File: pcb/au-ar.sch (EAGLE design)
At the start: 44 parts, among them U1 TPD12S520DBTR, U2 TPD12S521DBTR

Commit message: rearranged hdmi ports. removed end mounting holes to make room for dual ports on the end. added footprint for spi flash and added to schematic.
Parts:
- added R5: 47k, rcl:R-US_R0603
- added U$1: W25Q80DVSNIG, TDP12S521:W25Q80DVSNIG
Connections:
- net N$11 renamed SCL1_FPGA
- net N$12 renamed SDA1_FPGA
- net N$15 renamed HP1_FPGA
- removed net N$16: U2.5V_SUPPLY
- removed net N$17: U2.LV_SUPPLY
- removed net N$2: B1C.1
- removed net N$40: U1.5V_SUPPLY
- removed net N$41: U1.LV_SUPPLY
- removed net N$42: U1.CE_REMOTE_IN, U1.GND_2, U1.TMDS_GND_2, U1.TMDS_GND_3, U1.TMDS_GND_4, U1.TMDS_GND_5
- removed net N$43: U1.ESD_BYP, U1.GND, U1.TMDS_GND, U1.TMDS_GND_6, U1.TMDS_GND_7, U1.TMDS_GND_8
- removed net PIN: B1A.1
- new net 5V: B1A.1, B1A.50, B1B.1, B1B.50, B1C.1, B1C.50, B1D.1, B1D.50, U1.5V_SUPPLY, U2.5V_SUPPLY
- new net HP2_FPGA: U1.HOTPLUG_DET_IN
- new net SCL2_FPGA: U1.DDC_CLK_IN
- new net SDA2_FPGA: U1.DDC_DAT_IN
- new net SPI_CLK: U$1.CLK
- new net SPI_DI: U$1.DI
- new net SPI_DO: U$1.DO
- net 3V3: now also B1A.13, B1A.19, B1A.25, B1A.26, B1A.32, B1A.38, B1A.44, B1A.7, B1B.13, B1B.19, B1B.25, B1B.26, B1B.32, B1B.38, B1B.44, B1B.7, B1C.13, B1C.19, B1C.25, B1C.26, B1C.32, B1C.38, B1C.44, B1C.7, B1D.13, B1D.19, B1D.25, B1D.26, B1D.32, B1D.38, B1D.44, B1D.7, R5.2, U$1.HOLD, U$1.VCC, U$1.WP, U1.LV_SUPPLY, U2.LV_SUPPLY
- net CLK1_N: now also B1B.34
- net CLK1_P: now also B1B.33
- net CLK2_N: now also B1B.40
- net CLK2_P: now also B1B.39
- net D01_N: now also B1B.17
- net D01_P: now also B1B.18
- net D02_N: now also B1B.11
- net D02_P: now also B1B.12
- net D11_N: now also B1B.31
- net D11_P: now also B1B.30
- net D12_N: now also B1B.37
- net D12_P: now also B1B.36
- net D21_N: now also B1B.20
- net D21_P: now also B1B.21
- net D22_N: now also B1B.14
- net D22_P: now also B1B.15
- net GND: now also B1A.10, B1A.16, B1A.22, B1A.29, B1A.35, B1A.4, B1A.41, B1A.47, B1B.10, B1B.16, B1B.22, B1B.29, B1B.35, B1B.4, B1B.41, B1B.47, B1C.10, B1C.16, B1C.22, B1C.29, B1C.35, B1C.4, B1C.41, B1C.47, B1D.10, B1D.16, B1D.22, B1D.29, B1D.35, B1D.4, B1D.41, B1D.47, U$1.GND, U1.CE_REMOTE_IN, U1.ESD_BYP, U1.GND, U1.GND_2, U1.TMDS_GND, U1.TMDS_GND_2, U1.TMDS_GND_3, U1.TMDS_GND_4, U1.TMDS_GND_5, U1.TMDS_GND_6, U1.TMDS_GND_7, U1.TMDS_GND_8
- net LINE_1_1: now also B1A.24
- net LINE_1_2: now also B1A.21
- net LINE_1_3: now also B1A.18
- net LINE_1_4: now also B1A.15
- net LINE_2_1: now also B1A.12
- net LINE_2_2: now also B1A.9
- net LINE_2_3: now also B1A.6
- net LINE_2_4: now also B1A.3
- net N$1: now also R5.1, U$1.CS; no longer B1B.1

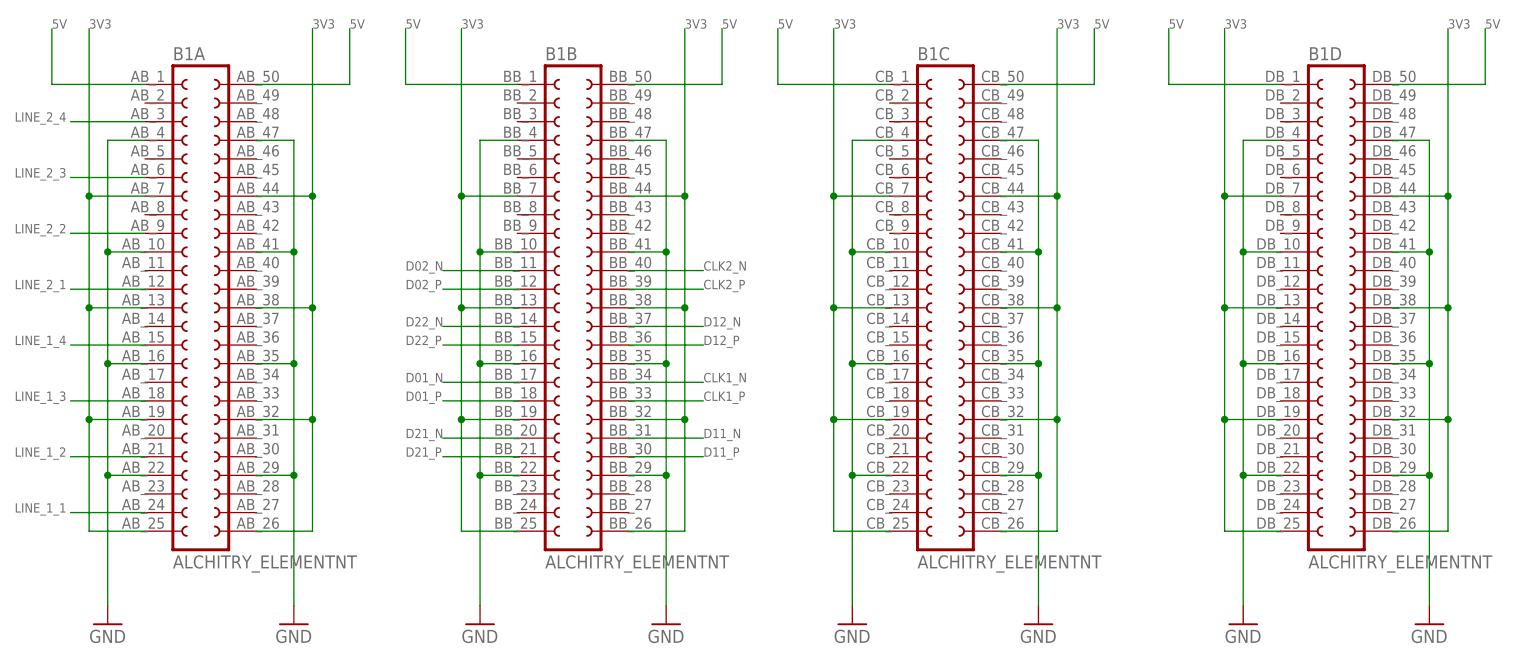
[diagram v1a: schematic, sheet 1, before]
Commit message: added remaining connections in schematic for spi flash and hdmi ddc bus
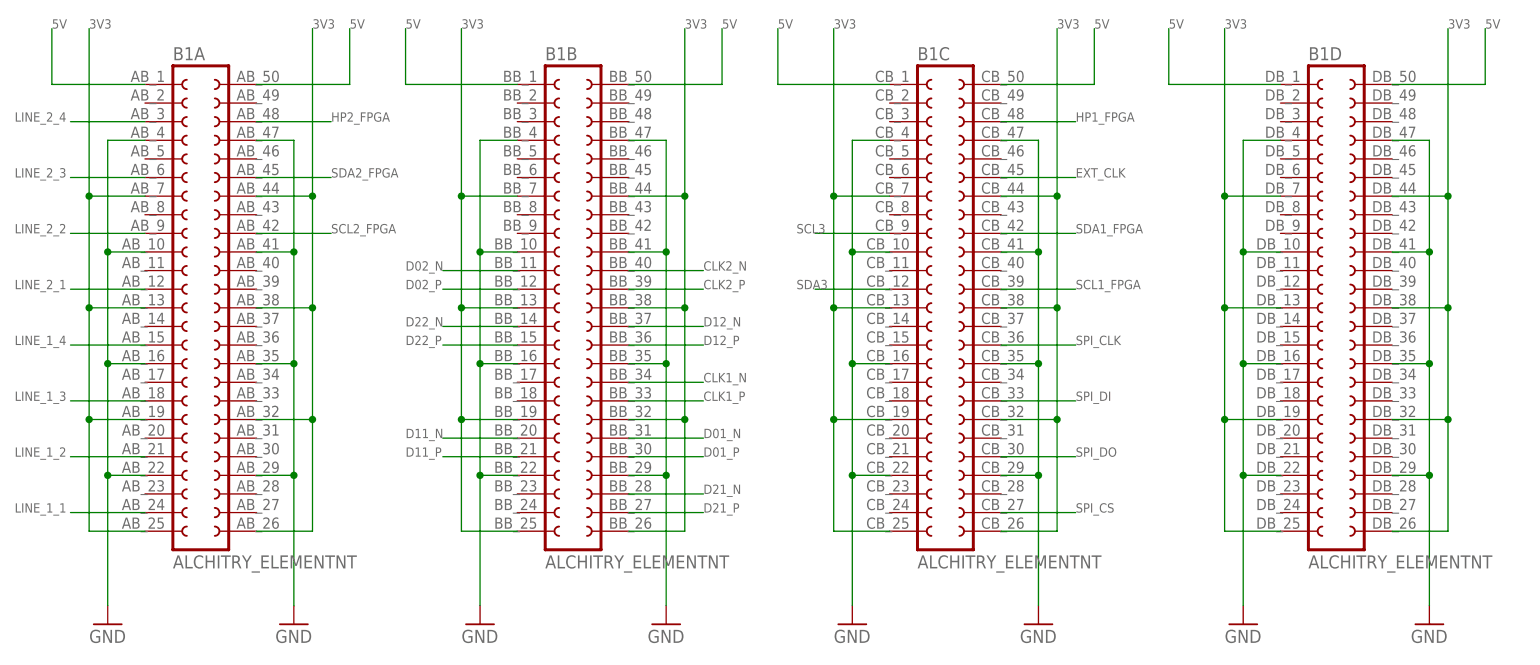
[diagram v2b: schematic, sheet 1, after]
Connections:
- removed net N$1: R5.1, U$1.CS
- new net EXT_CLK: B1C.45
- new net SCL3: B1C.9
- new net SDA3: B1C.12
- new net SPI_CS: B1C.27, R5.1, U$1.CS
- net D01_N: now also B1B.31; no longer B1B.17
- net D01_P: now also B1B.30; no longer B1B.18
- net D11_N: now also B1B.20; no longer B1B.31
- net D11_P: now also B1B.21; no longer B1B.30
- net D21_N: now also B1B.28; no longer B1B.20
- net D21_P: now also B1B.27; no longer B1B.21
- net HP1_FPGA: now also B1C.48
- net HP2_FPGA: now also B1A.48
- net SCL1_FPGA: now also B1C.39
- net SCL2_FPGA: now also B1A.42
- net SDA1_FPGA: now also B1C.42
- net SDA2_FPGA: now also B1A.45
- net SPI_CLK: now also B1C.36
- net SPI_DI: now also B1C.33
- net SPI_DO: now also B1C.30
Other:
- moved on the sheet: R5

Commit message: started routing hdmi tmds signals. had to make min hole size .2mm
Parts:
- added C1: 1uF, rcl:C-USC0603
- added C11, C12, C2, C3, C4, C5, C6, C7, C8: 0.1uF, rcl:C-USC0603
- added R27, R6: 3k, rcl:R-US_R0603
- added R28, R37: 1k, rcl:R-US_R0603
- added R31, R32, R33, R34, R43, R44, R46, R47, R48, R49: 47k, rcl:R-US_R0603
- added R35: NP, rcl:R-US_R0603
- added R36, R40, R41: 10k, rcl:R-US_R0603
- added R38, R39: 27k, rcl:R-US_R0603
- added R42, R45: 100k, rcl:R-US_R0603
- added U$2: SI514, lupa300-components:SI514
- C10, C9: value 1uF -> 0.1uF
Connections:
- removed net N$55: U2.GND_2, U2.TMDS_GND_2, U2.TMDS_GND_3, U2.TMDS_GND_4, U2.TMDS_GND_5
- removed net N$56: U2.ESD_BYP, U2.GND, U2.TMDS_GND, U2.TMDS_GND_6, U2.TMDS_GND_7, U2.TMDS_GND_8
- new net CEC1: HDMI_1.13, R39.2, U2.CE_REMOTE_OUT
- new net CEC1_FPGA: B1C.3, R43.1, U2.CE_REMOTE_IN
- new net CEC2: HDMI_2.13, R38.2, U1.CE_REMOTE_OUT
- new net CEC2_FPGA: B1A.39, R49.1, U1.CE_REMOTE_IN
- new net N$1: C5.1, U1.ESD_BYP
- new net N$11: HDMI_1.14, R36.2
- new net N$12: C3.1, R41.1, U1.LV_SUPPLY
- new net N$15: C7.1, R40.1, U2.LV_SUPPLY
- new net N$16: C8.1, U2.ESD_BYP
- new net N$2: HDMI_2.14, R35.2
- net 3V3: now also C1.1, C2.1, R27.2, R38.1, R39.1, R40.2, R41.2, R42.2, R43.2, R44.2, R45.2, R46.2, R47.2, R48.2, R49.2, R6.2, U$2.VDD; no longer U1.LV_SUPPLY, U2.LV_SUPPLY
- net 5V: now also C4.1, C6.1, R31.1, R32.1, R33.1, R34.1
- net 5VHDMI1: now also C11.1, R37.1
- net 5VHDMI2: now also C12.1, R28.1
- net EXT_CLK: now also U$2.CLK
- net GND: now also C1.2, C11.2, C12.2, C2.2, C3.2, C4.2, C5.2, C6.2, C7.2, C8.2, R35.1, R36.1, U$2.GND, U2.GND, U2.GND_2, U2.TMDS_GND, U2.TMDS_GND_2, U2.TMDS_GND_3, U2.TMDS_GND_4, U2.TMDS_GND_5, U2.TMDS_GND_6, U2.TMDS_GND_7, U2.TMDS_GND_8; no longer U1.CE_REMOTE_IN, U1.ESD_BYP
- net HP1: now also R37.2
- net HP1_FPGA: now also R42.1
- net HP2: now also R28.2
- net HP2_FPGA: now also R45.1
- net SCL1: now also R33.2
- net SCL1_FPGA: now also R44.1
- net SCL2: now also R31.2
- net SCL2_FPGA: now also R48.1
- net SCL3: now also R27.1, U$2.SCL
- net SDA1: now also R34.2
- net SDA1_FPGA: now also R46.1
- net SDA2: now also R32.2
- net SDA2_FPGA: now also R47.1
- net SDA3: now also B1C.6, R6.1, U$2.SDA; no longer B1C.12

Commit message: reorganized hdmi pins, hdmi routing almost done
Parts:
- removed C1: 1uF, rcl:C-USC0603
- removed C2: 0.1uF, rcl:C-USC0603
- removed R27, R6: 3k, rcl:R-US_R0603
- removed U$2: SI514, lupa300-components:SI514
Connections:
- removed net EXT_CLK: B1C.45, U$2.CLK
- removed net SCL3: B1C.9, R27.1, U$2.SCL
- removed net SDA3: B1C.6, R6.1, U$2.SDA
- net 3V3: no longer C1.1, C2.1, R27.2, R6.2, U$2.VDD
- net D02_N: now also B1B.49; no longer B1B.11
- net D02_P: now also B1B.48; no longer B1B.12
- net D12_N: now also B1B.46; no longer B1B.37
- net D12_P: now also B1B.45; no longer B1B.36
- net D22_N: now also B1B.5; no longer B1B.14
- net D22_P: now also B1B.6; no longer B1B.15
- net GND: no longer C1.2, C2.2, U$2.GND
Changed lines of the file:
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@@
 <part name="U$1" library="TDP12S521" deviceset="W25Q80DVSNIG" device=""/>
 <part name="R5" library="rcl" library_urn="urn:adsk.eagle:library:334" deviceset="R-US_" device="R0603" package3d_urn="urn:adsk.eagle:package:23555/3" value="47k"/>
-<part name="U$2" library="lupa300-components" deviceset="SI514" device=""/>
-<part name="R6" library="rcl" library_urn="urn:adsk.eagle:library:334" deviceset="R-US_" device="R0603" package3d_urn="urn:adsk.eagle:package:23555/3" value="3k"/>
-<part name="R27" library="rcl" library_urn="urn:adsk.eagle:library:334" deviceset="R-US_" device="R0603" package3d_urn="urn:adsk.eagle:package:23555/3" value="3k"/>
-<part name="C1" library="rcl" library_urn="urn:adsk.eagle:library:334" deviceset="C-US" device="C0603" package3d_urn="urn:adsk.eagle:package:23616/2" value="1uF"/>
-<part name="C2" library="rcl" library_urn="urn:adsk.eagle:library:334" deviceset="C-US" device="C0603" package3d_urn="urn:adsk.eagle:package:23616/2" value="0.1uF"/>
 <part name="C3" library="rcl" library_urn="urn:adsk.eagle:library:334" deviceset="C-US" device="C0603" package3d_urn="urn:adsk.eagle:package:23616/2" value="0.1uF"/>
 <part name="C4" library="rcl" library_urn="urn:adsk.eagle:library:334" deviceset="C-US" device="C0603" package3d_urn="urn:adsk.eagle:package:23616/2" value="0.1uF"/>
@@
 <net name="D02_N" class="1">
 <segment>
-<pinref part="B1" gate="B" pin="11"/>
-<wire x1="83.82" y1="66.04" x2="73.66" y2="66.04" width="0.1524" layer="91"/>
-<label x="68.58" y="66.04" size="1.27" layer="95"/>
+<pinref part="B1" gate="B" pin="49"/>
+<wire x1="99.06" y1="88.9" x2="109.22" y2="88.9" width="0.1524" layer="91"/>
+<label x="109.22" y="88.9" size="1.27" layer="95"/>
 </segment>
 </net>
 <net name="D02_P" class="1">
 <segment>
-<pinref part="B1" gate="B" pin="12"/>
-<wire x1="83.82" y1="63.5" x2="73.66" y2="63.5" width="0.1524" layer="91"/>
-<label x="68.58" y="63.5" size="1.27" layer="95"/>
+<pinref part="B1" gate="B" pin="48"/>
+<wire x1="99.06" y1="86.36" x2="109.22" y2="86.36" width="0.1524" layer="91"/>
+<label x="109.22" y="86.36" size="1.27" layer="95"/>
 </segment>
 </net>
 <net name="D22_N" class="1">
 <segment>
-<pinref part="B1" gate="B" pin="14"/>
-<wire x1="83.82" y1="58.42" x2="73.66" y2="58.42" width="0.1524" layer="91"/>
-<label x="68.58" y="58.42" size="1.27" layer="95"/>
+<pinref part="B1" gate="B" pin="5"/>
+<wire x1="83.82" y1="81.28" x2="73.66" y2="81.28" width="0.1524" layer="91"/>
+<label x="68.58" y="81.28" size="1.27" layer="95"/>
 </segment>
 </net>
 <net name="D22_P" class="1">
 <segment>
-<pinref part="B1" gate="B" pin="15"/>
-<wire x1="83.82" y1="55.88" x2="73.66" y2="55.88" width="0.1524" layer="91"/>
-<label x="68.58" y="55.88" size="1.27" layer="95"/>
+<pinref part="B1" gate="B" pin="6"/>
+<wire x1="83.82" y1="78.74" x2="73.66" y2="78.74" width="0.1524" layer="91"/>
+<label x="68.58" y="78.74" size="1.27" layer="95"/>
 </segment>
 </net>
 <net name="D12_N" class="1">
 <segment>
-<pinref part="B1" gate="B" pin="37"/>
-<wire x1="99.06" y1="58.42" x2="109.22" y2="58.42" width="0.1524" layer="91"/>
-<label x="109.22" y="58.42" size="1.27" layer="95"/>
+<pinref part="B1" gate="B" pin="46"/>
+<wire x1="99.06" y1="81.28" x2="109.22" y2="81.28" width="0.1524" layer="91"/>
+<label x="109.22" y="81.28" size="1.27" layer="95"/>
 </segment>
 </net>
 <net name="D12_P" class="1">
 <segment>
-<pinref part="B1" gate="B" pin="36"/>
-<wire x1="99.06" y1="55.88" x2="109.22" y2="55.88" width="0.1524" layer="91"/>
-<label x="109.22" y="55.88" size="1.27" layer="95"/>
+<pinref part="B1" gate="B" pin="45"/>
+<wire x1="99.06" y1="78.74" x2="109.22" y2="78.74" width="0.1524" layer="91"/>
+<label x="109.22" y="78.74" size="1.27" layer="95"/>
 </segment>
 </net>
@@
 </segment>
 </net>
-<net name="EXT_CLK" class="0">
-<segment>
-<pinref part="B1" gate="C" pin="45"/>
-<wire x1="149.86" y1="78.74" x2="160.02" y2="78.74" width="0.1524" layer="91"/>
-<label x="160.02" y="78.74" size="1.27" layer="95"/>
-</segment>
-</net>
-<net name="SCL3" class="0">
-<segment>
-<pinref part="B1" gate="C" pin="9"/>
-<wire x1="134.62" y1="71.12" x2="124.46" y2="71.12" width="0.1524" layer="91"/>
-<label x="121.92" y="71.12" size="1.27" layer="95"/>
-</segment>
-</net>
 <net name="D01_N" class="1">
 <segment>
@@
 <wire x1="83.82" y1="40.64" x2="73.66" y2="40.64" width="0.1524" layer="91"/>
 <label x="68.58" y="40.64" size="1.27" layer="95"/>
-</segment>
-</net>
-<net name="SDA3" class="0">
-<segment>
-<pinref part="B1" gate="C" pin="6"/>
-<wire x1="134.62" y1="78.74" x2="124.46" y2="78.74" width="0.1524" layer="91"/>
-<label x="121.92" y="78.74" size="1.27" layer="95"/>
 </segment>
 </net>
@@
 </segment>
 </net>
-</nets>
-</sheet>
-<sheet>
-<description>Programmable Oscillator</description>
-<plain>
-</plain>
-<instances>
-<instance part="U$2" gate="G$1" x="33.02" y="30.48" smashed="yes">
-<attribute name="NAME" x="22.86" y="43.18" size="1.778" layer="95"/>
-<attribute name="VALUE" x="35.56" y="43.18" size="1.778" layer="96"/>
-</instance>
-<instance part="R6" gate="G$1" x="2.54" y="40.64" smashed="yes" rot="R90">
-<attribute name="NAME" x="1.0414" y="36.83" size="1.778" layer="95" rot="R90"/>
-<attribute name="VALUE" x="5.842" y="36.83" size="1.778" layer="96" rot="R90"/>
-</instance>
-<instance part="R27" gate="G$1" x="7.62" y="40.64" smashed="yes" rot="R90">
-<attribute name="NAME" x="6.1214" y="36.83" size="1.778" layer="95" rot="R90"/>
-<attribute name="VALUE" x="10.922" y="36.83" size="1.778" layer="96" rot="R90"/>
-</instance>
-<instance part="C1" gate="G$1" x="33.02" y="58.42" smashed="yes">
-<attribute name="NAME" x="34.036" y="59.055" size="1.778" layer="95"/>
-<attribute name="VALUE" x="34.036" y="54.229" size="1.778" layer="96"/>
-</instance>
-<instance part="C2" gate="G$1" x="43.18" y="58.42" smashed="yes">
-<attribute name="NAME" x="44.196" y="59.055" size="1.778" layer="95"/>
-<attribute name="VALUE" x="44.196" y="54.229" size="1.778" layer="96"/>
-</instance>
-</instances>
-<busses>
-</busses>
-<nets>
-<net name="EXT_CLK" class="0">
-<segment>
-<pinref part="U$2" gate="G$1" pin="CLK"/>
-<wire x1="45.72" y1="35.56" x2="53.34" y2="35.56" width="0.1524" layer="91"/>
-<label x="53.34" y="35.56" size="1.27" layer="95"/>
-</segment>
-</net>
-<net name="GND" class="0">
-<segment>
-<pinref part="U$2" gate="G$1" pin="GND"/>
-<wire x1="20.32" y1="22.86" x2="15.24" y2="22.86" width="0.1524" layer="91"/>
-<wire x1="15.24" y1="22.86" x2="15.24" y2="10.16" width="0.1524" layer="91"/>
-<label x="15.24" y="10.16" size="1.27" layer="95"/>
-</segment>
-<segment>
-<pinref part="C2" gate="G$1" pin="2"/>
-<wire x1="43.18" y1="53.34" x2="43.18" y2="50.8" width="0.1524" layer="91"/>
-<wire x1="43.18" y1="50.8" x2="38.1" y2="50.8" width="0.1524" layer="91"/>
-<pinref part="C1" gate="G$1" pin="2"/>
-<wire x1="38.1" y1="50.8" x2="33.02" y2="50.8" width="0.1524" layer="91"/>
-<wire x1="33.02" y1="50.8" x2="33.02" y2="53.34" width="0.1524" layer="91"/>
-<wire x1="38.1" y1="50.8" x2="38.1" y2="48.26" width="0.1524" layer="91"/>
-<junction x="38.1" y="50.8"/>
-<label x="38.1" y="48.26" size="1.27" layer="95"/>
-</segment>
-</net>
-<net name="3V3" class="0">
-<segment>
-<pinref part="U$2" gate="G$1" pin="VDD"/>
-<wire x1="20.32" y1="38.1" x2="15.24" y2="38.1" width="0.1524" layer="91"/>
-<wire x1="15.24" y1="38.1" x2="15.24" y2="48.26" width="0.1524" layer="91"/>
-<pinref part="R27" gate="G$1" pin="2"/>
-<wire x1="7.62" y1="45.72" x2="7.62" y2="48.26" width="0.1524" layer="91"/>
-<wire x1="7.62" y1="48.26" x2="15.24" y2="48.26" width="0.1524" layer="91"/>
-<pinref part="R6" gate="G$1" pin="2"/>
-<wire x1="2.54" y1="45.72" x2="2.54" y2="48.26" width="0.1524" layer="91"/>
-<wire x1="2.54" y1="48.26" x2="7.62" y2="48.26" width="0.1524" layer="91"/>
-<junction x="7.62" y="48.26"/>
-<wire x1="7.62" y1="48.26" x2="7.62" y2="50.8" width="0.1524" layer="91"/>
-<label x="7.62" y="50.8" size="1.27" layer="95"/>
-</segment>
-<segment>
-<pinref part="C1" gate="G$1" pin="1"/>
-<wire x1="33.02" y1="60.96" x2="33.02" y2="63.5" width="0.1524" layer="91"/>
-<wire x1="33.02" y1="63.5" x2="38.1" y2="63.5" width="0.1524" layer="91"/>
-<pinref part="C2" gate="G$1" pin="1"/>
-<wire x1="38.1" y1="63.5" x2="43.18" y2="63.5" width="0.1524" layer="91"/>
-<wire x1="43.18" y1="63.5" x2="43.18" y2="60.96" width="0.1524" layer="91"/>
-<wire x1="38.1" y1="63.5" x2="38.1" y2="66.04" width="0.1524" layer="91"/>
-<junction x="38.1" y="63.5"/>
-<label x="38.1" y="66.04" size="1.27" layer="95"/>
-</segment>
-</net>
-<net name="SDA3" class="0">
-<segment>
-<pinref part="U$2" gate="G$1" pin="SDA"/>
-<wire x1="20.32" y1="33.02" x2="2.54" y2="33.02" width="0.1524" layer="91"/>
-<pinref part="R6" gate="G$1" pin="1"/>
-<wire x1="2.54" y1="33.02" x2="-5.08" y2="33.02" width="0.1524" layer="91"/>
-<wire x1="2.54" y1="35.56" x2="2.54" y2="33.02" width="0.1524" layer="91"/>
-<junction x="2.54" y="33.02"/>
-<label x="-10.16" y="33.02" size="1.27" layer="95"/>
-</segment>
-</net>
-<net name="SCL3" class="0">
-<segment>
-<pinref part="U$2" gate="G$1" pin="SCL"/>
-<wire x1="20.32" y1="27.94" x2="7.62" y2="27.94" width="0.1524" layer="91"/>
-<pinref part="R27" gate="G$1" pin="1"/>
-<wire x1="7.62" y1="27.94" x2="-5.08" y2="27.94" width="0.1524" layer="91"/>
-<wire x1="7.62" y1="35.56" x2="7.62" y2="27.94" width="0.1524" layer="91"/>
-<junction x="7.62" y="27.94"/>
-<label x="-10.16" y="27.94" size="1.27" layer="95"/>
-</segment>
-</net>

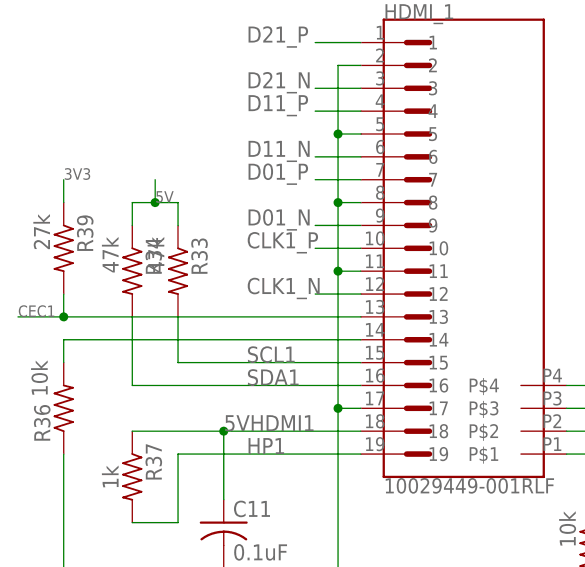
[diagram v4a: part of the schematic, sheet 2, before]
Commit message: routed hdmi, need to route low speed signals
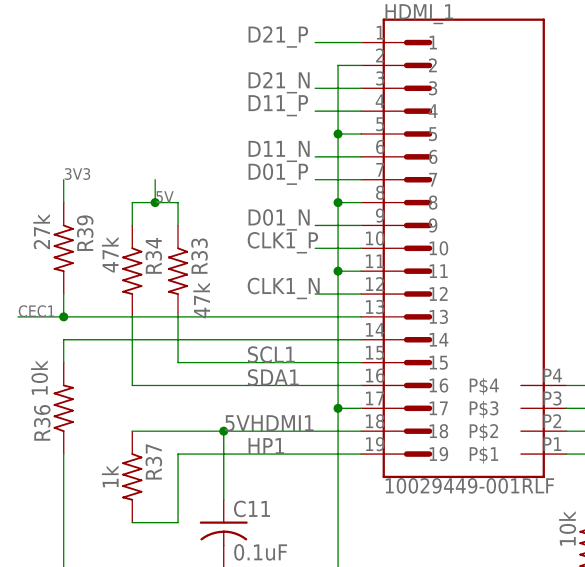
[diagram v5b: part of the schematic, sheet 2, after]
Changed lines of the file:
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@@
 <instance part="R33" gate="G$1" x="5.08" y="66.04" smashed="yes" rot="R270">
 <attribute name="NAME" x="6.5786" y="69.85" size="1.778" layer="95" rot="R270"/>
-<attribute name="VALUE" x="1.778" y="69.85" size="1.778" layer="96" rot="R270"/>
+<attribute name="VALUE" x="6.858" y="64.77" size="1.778" layer="96" rot="R270"/>
 </instance>
 <instance part="R34" gate="G$1" x="0" y="66.04" smashed="yes" rot="R270">
